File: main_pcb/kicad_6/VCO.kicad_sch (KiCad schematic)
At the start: 35 parts, among them J201 aux_FM_in, SW201 SR1712F-0204, U1 SSI2130

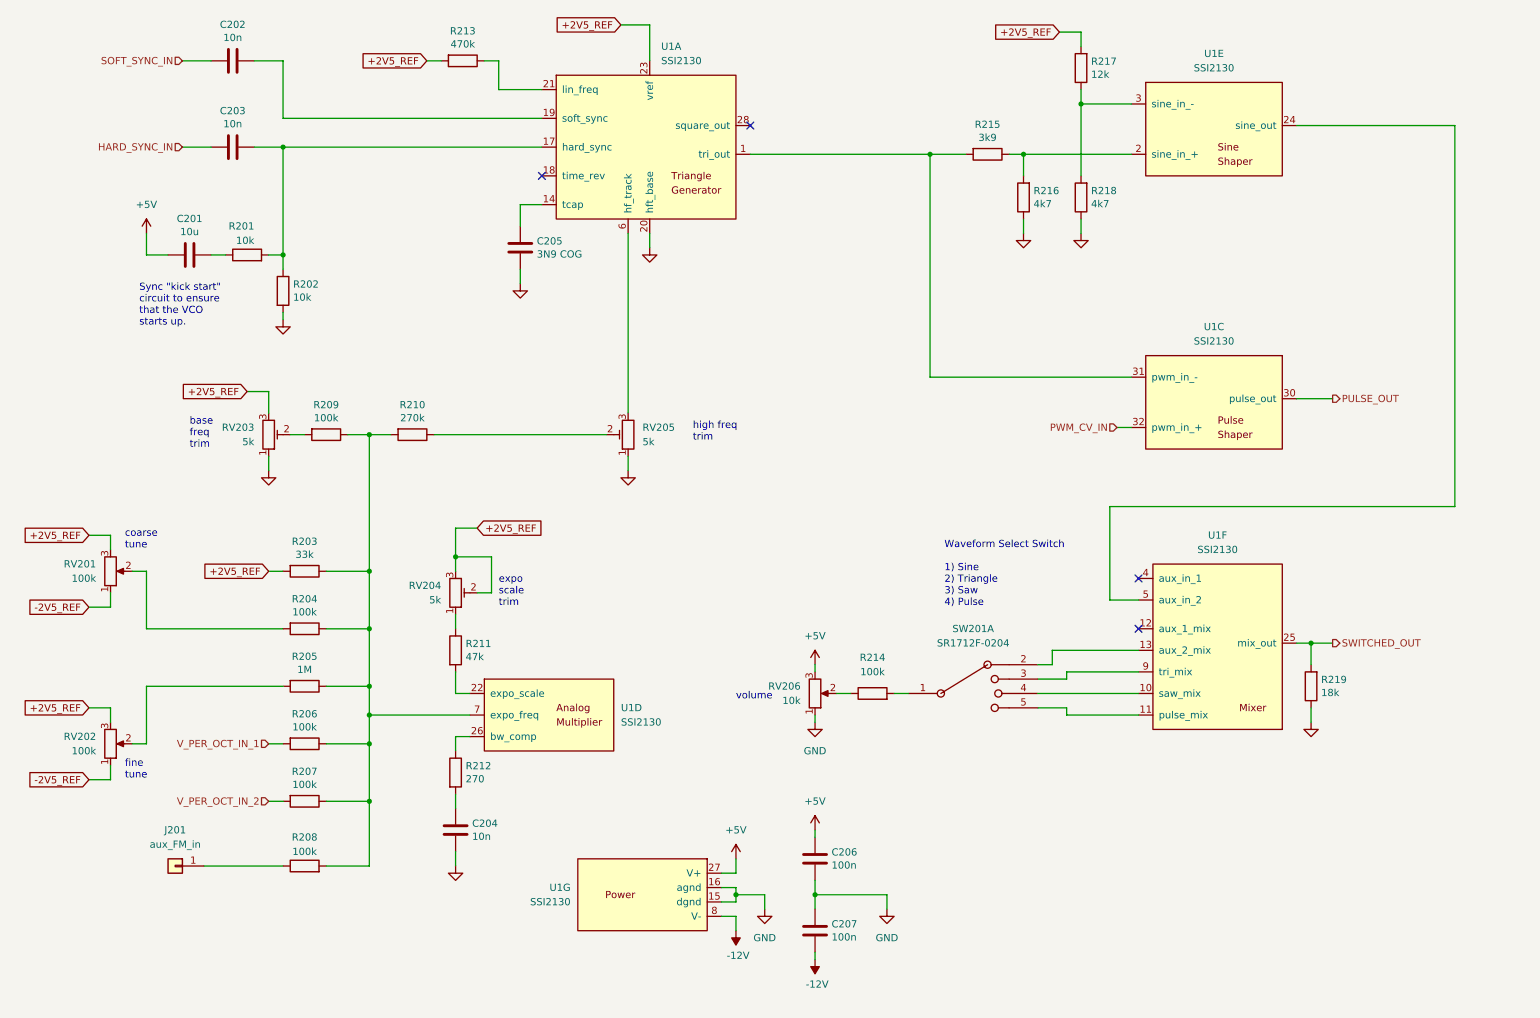
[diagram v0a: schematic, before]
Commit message: Update rev 0.1, fix VCA tails, add local 2v5 regs, change some pot footprints
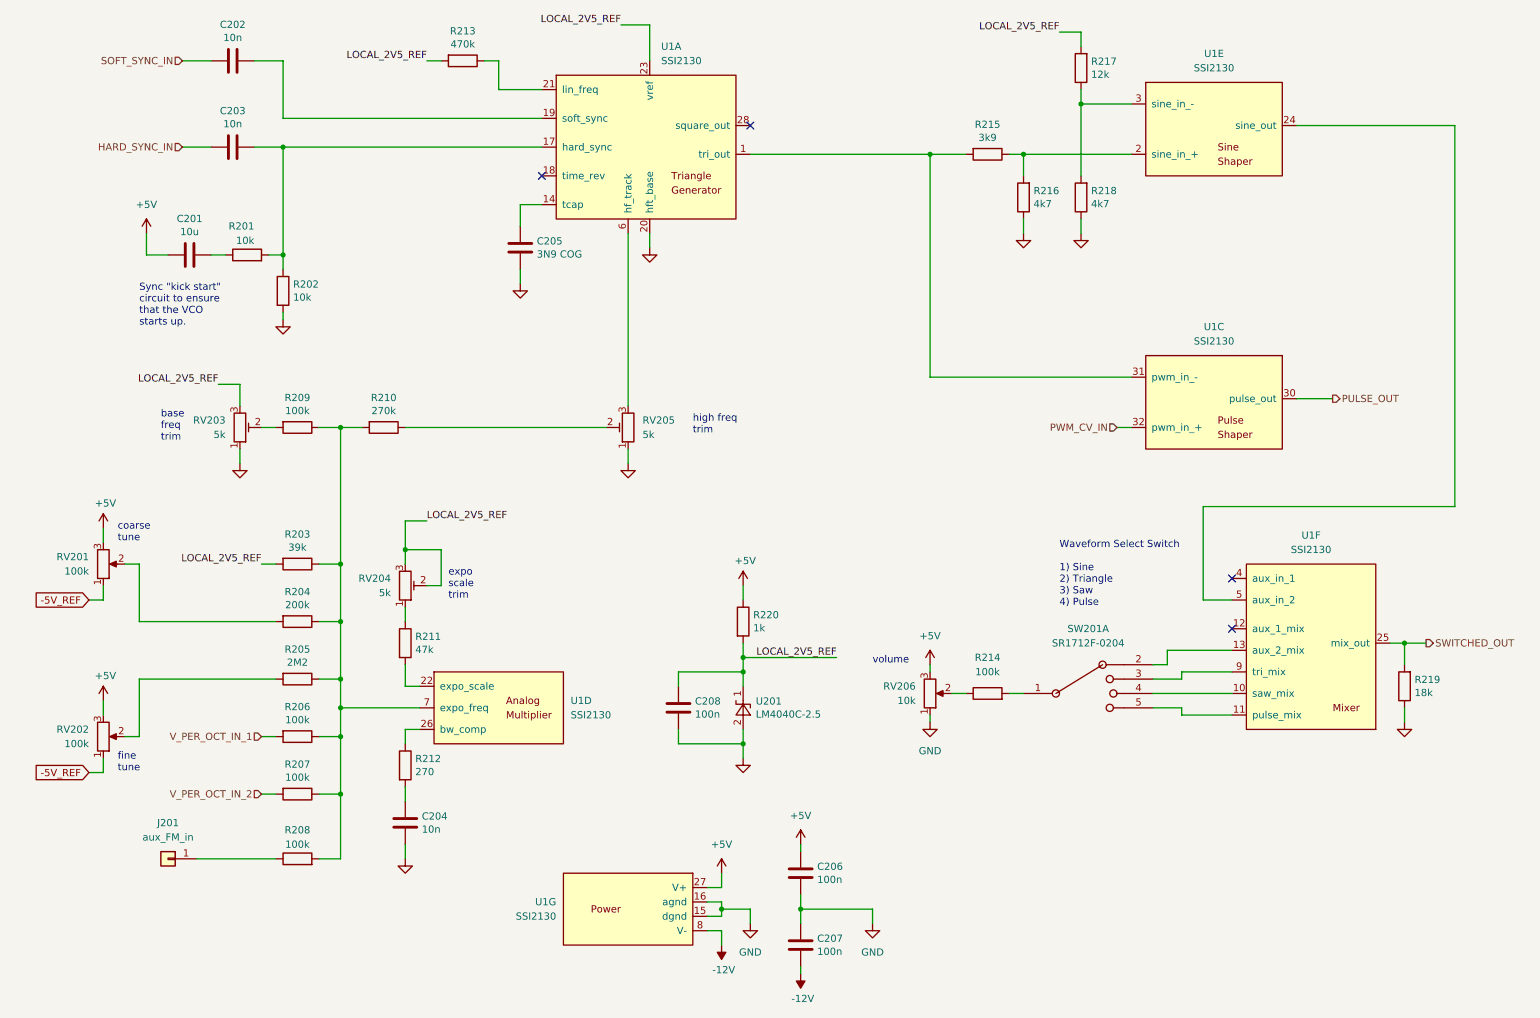
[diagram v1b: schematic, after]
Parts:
- added C208: 100n, Capacitor_SMD:C_0603_1608Metric, symbol Device:C
- added R220: 1k, Resistor_SMD:R_0603_1608Metric, symbol Device:R
- added U201: LM4040C-2.5, Package_TO_SOT_SMD:SOT-23, symbol Reference_Voltage:LM4040DBZ-2.5
- J201: now left out of the parts list
- R203: value 33k -> 39k
- R204: value 100k -> 200k
- R205: value 1M -> 2M2
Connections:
- net +5V: now also RV201.3, RV202.3, R220.1
- net GND: now also C208.2, U201.2 (A)
- net +2V5_REF renamed LOCAL_2V5_REF
- net LOCAL_2V5_REF: now also C208.1, R220.2, U201.1 (K); no longer RV201.3, RV202.3
- net -2V5_REF renamed -5V_REF
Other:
- moved on the sheet: C204, C206, C207, J201, R203, R204, R205, R206, R207, R208, R209, R210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

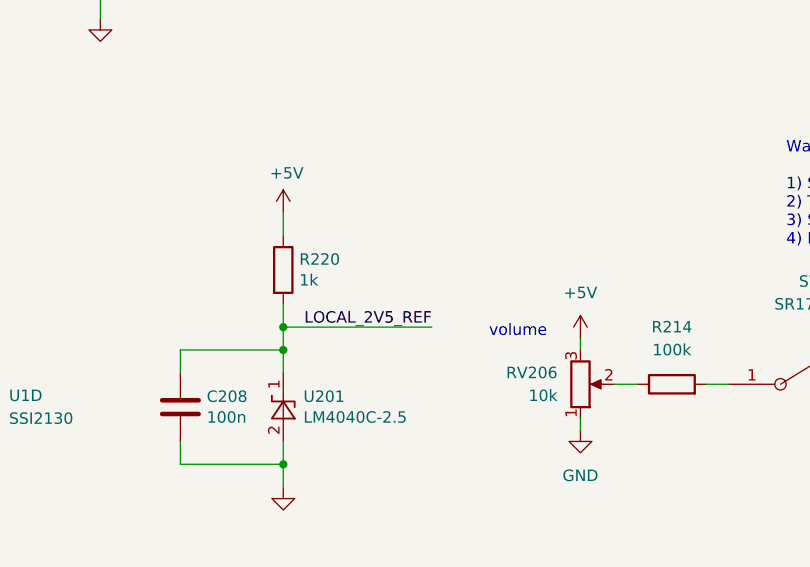
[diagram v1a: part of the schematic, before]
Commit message: Add mod-wheel VCA, fix occasional VCO freq locking
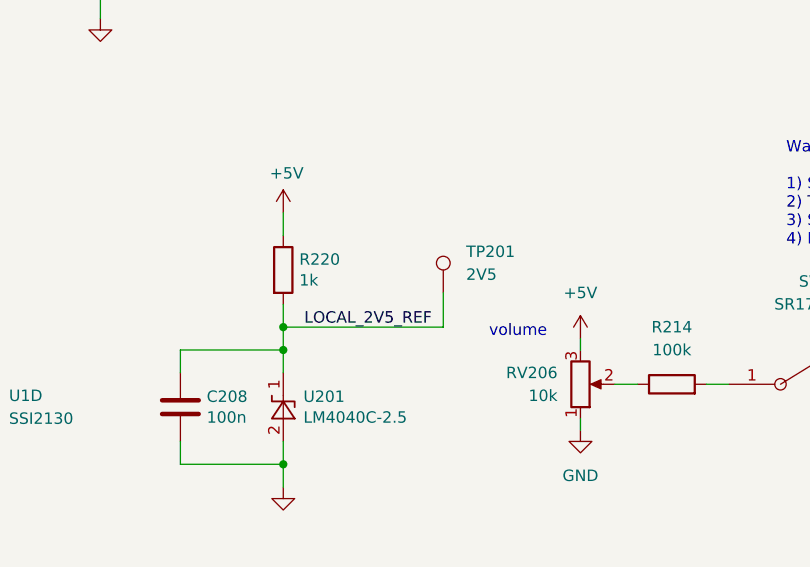
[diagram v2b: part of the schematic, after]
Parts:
- added TP201: 2V5, TestPoint:TestPoint_Keystone_5000-5004_Miniature, symbol Connector:TestPoint
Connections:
- net LOCAL_2V5_REF: now also TP201.1
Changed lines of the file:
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@@
   (title_block
     (title "Micro-Pico Tiny Monosynth")
-    (date "2022-08-28")
-    (rev "0.1")
+    (date "2022-10-06")
+    (rev "1.0")
     (comment 1 "creativecommons.org/licences/by/4.0")
     (comment 2 "Licence: CC by 4.0")
@@
     (stroke (width 0) (type default) (color 0 0 0 0))
   )
-  (wire (pts (xy 144.78 134.62) (xy 161.29 134.62))
+  (wire (pts (xy 144.78 134.62) (xy 162.56 134.62))
     (stroke (width 0) (type default) (color 0 0 0 0))
   )
@@
   )
   (wire (pts (xy 261.62 132.08) (xy 265.43 132.08))
+    (stroke (width 0) (type default) (color 0 0 0 0))
+  )
+  (wire (pts (xy 162.56 130.81) (xy 162.56 134.62))
     (stroke (width 0) (type default) (color 0 0 0 0))
   )
@@
     (pin "2")
   )
+  (symbol (lib_id "Connector:TestPoint") (at 162.56 130.81 0) (unit 1)
+    (in_bom no) (on_board yes) (fields_autoplaced)
+    (property "Reference" "TP201" (id 0) (at 165.1 126.2379 0)
+      (effects (font (size 1.27 1.27)) (justify left))
+    )
+    (property "Value" "2V5" (id 1) (at 165.1 128.7779 0)
+      (effects (font (size 1.27 1.27)) (justify left))
+    )
+    (property "Footprint" "TestPoint:TestPoint_Keystone_5000-5004_Miniature" (id 2) (at 167.64 130.81 0)
+      (effects (font (size 1.27 1.27)) hide)
+    )
+    (property "Datasheet" "~" (id 3) (at 167.64 130.81 0)
+      (effects (font (size 1.27 1.27)) hide)
+    )
+    (pin "1")
+  )
   (symbol (lib_id "custom_symbols:SSI2130") (at 227.33 88.9 0) (unit 3)
